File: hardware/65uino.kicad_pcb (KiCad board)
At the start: 2 copper layers, 74.9 x 53.3 mm, 58 parts, among them J1 Barrel_Jack_MountingPin, J2 USB_B_Micro, J3 OLED, SW1 RST, SW2 BTN, U1 R6507, U2 NC/74HC04, U3 6532, U4 w27C512, U5 MIC5504-3.3YM5, U6 LM1117-5.0, U7 SN74LVC1G14DBVR, X1 1MHz, Y1 NC/1Mhz

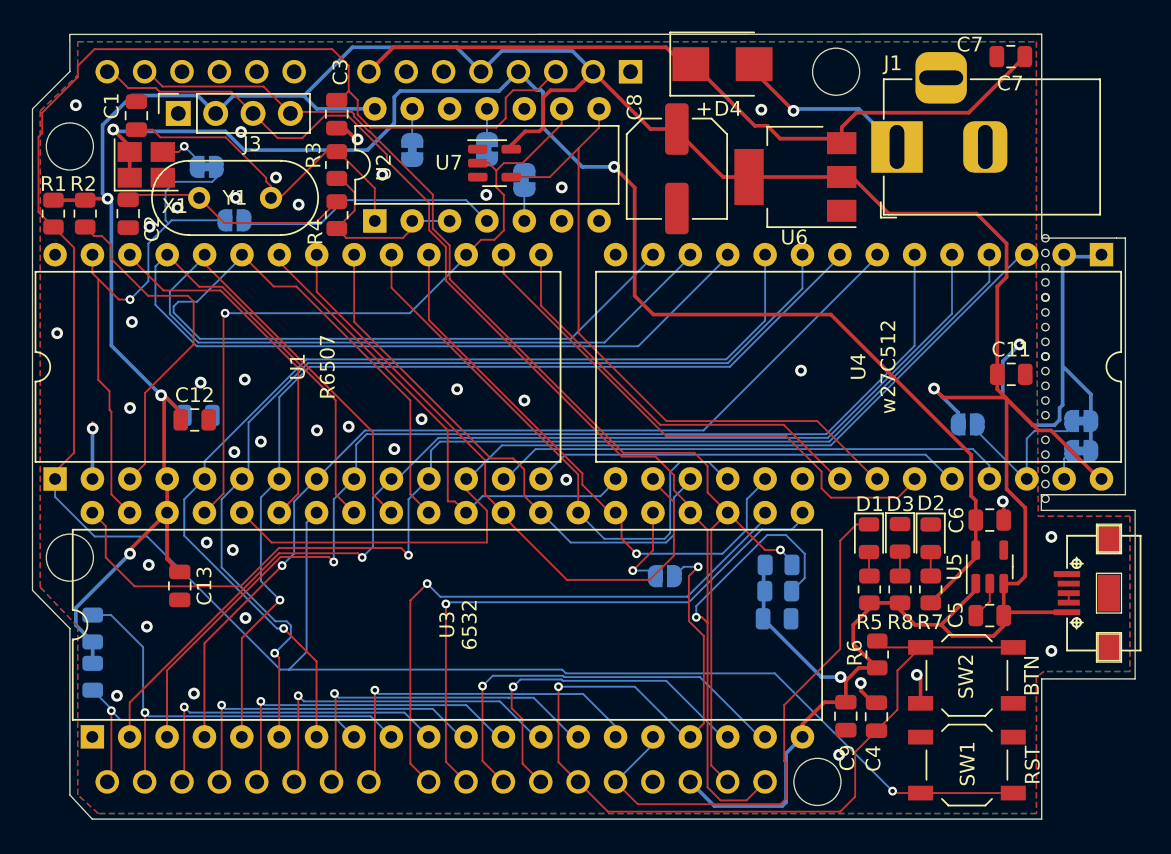
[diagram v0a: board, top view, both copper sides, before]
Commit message: Manufacturing improvements
MicroUSB changed to Amphenol 10118194
5V regulator capacitors changed to 1206 10uF
LCSC Parts numbers added
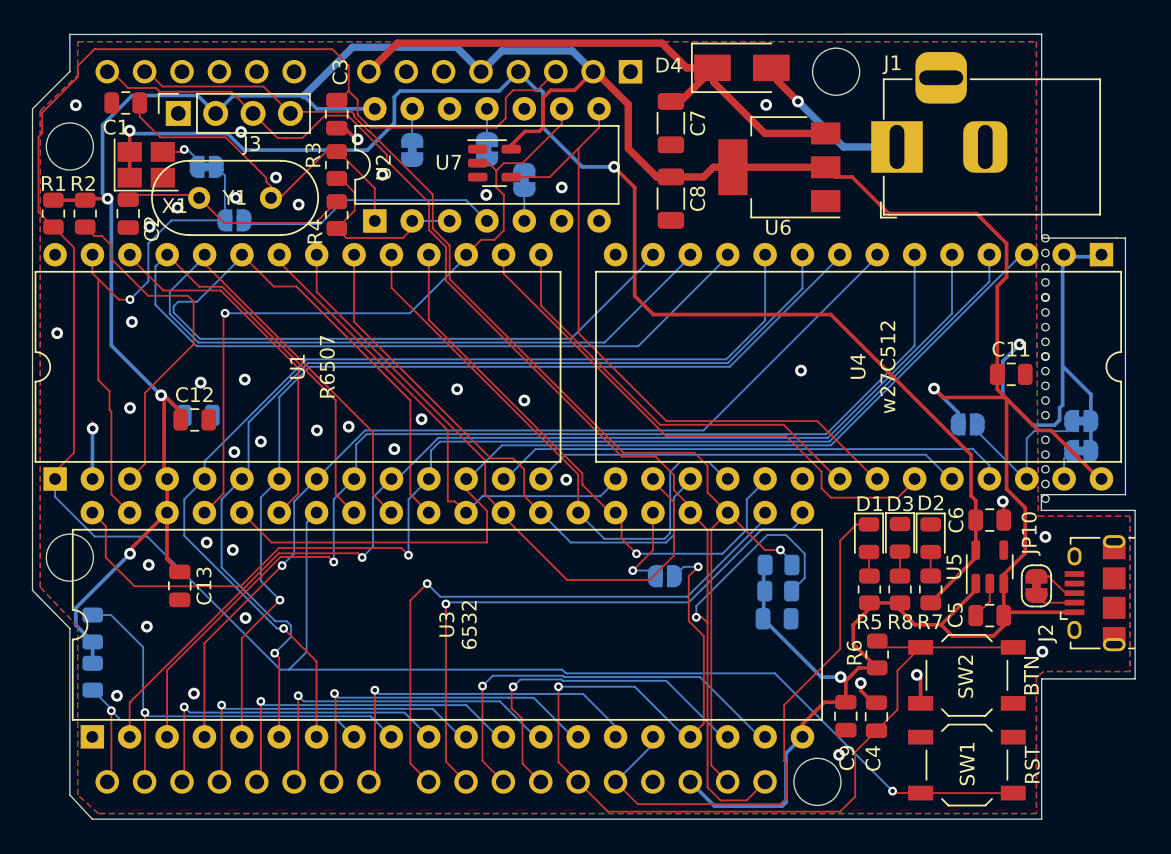
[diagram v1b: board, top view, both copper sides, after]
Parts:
- added JP10: SolderJumper_2_Bridged, Jumper:SolderJumper-2_P1.3mm_Bridged_RoundedPad1.0x1.5mm, F.Cu at (170.2, 86.0)
- A1: value Arduino Footprint -> NC/Arduino Footprint
- C7: value C_Input -> 10uF; footprint Capacitor_SMD:C_0805_2012Metric -> Capacitor_SMD:C_1206_3216Metric
- C8: value 47uF -> 10uF; footprint Capacitor_SMD:CP_Elec_6.3x7.7 -> Capacitor_SMD:C_1206_3216Metric
- D1: value LED -> GREEN LED
- D2: value LED -> RED LED
- D3: value LED -> WHITE LED
- D4: footprint Diode_SMD:D_SMB -> Diode_SMD:D_SMA
- J2: footprint Connector_USB:USB-B-MICRO-SMD_V03-fixed -> Connector_USB:USB_Micro-B_Amphenol_10118194_Horizontal
- moved C7 23.5 mm to (145.3, 54.6), turned to -90 degrees
- moved C8 2.07 mm to (145.3, 59.7)
- moved D4 1.35 mm to (150.2, 50.8)
- moved U6 1.28 mm to (152.7, 57.6)
- moved C1 1.13 mm to (108.3, 53.2), turned to 180 degrees
- moved J2 0.94 mm to (174.2, 86.5), turned to 90 degrees
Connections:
- J2 pad 3: Net-(J2-Pad2) -> Net-(J2-Pad3)
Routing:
- net /VIN: track 49.9 -> 38.2 mm
- net /PHI0: track 38.3 -> 35.4 mm
- net Net-(J2-Pad3): track 0.00 -> 2.45 mm
- net +5V: track 238.4 -> 240.8 mm
- net Net-(J2-Pad2): track 0.65 -> 2.79 mm
- net +3V3: track 92.9 -> 91.2 mm
- net Net-(D4-Pad2): track 12.2 -> 10.9 mm
- net Net-(C1-Pad1): track 21.9 -> 22.9 mm
- net Net-(U3-Pad25): track 6.19 -> 5.65 mm

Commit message: Minor PCB update
Gerbers regenerated
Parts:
- moved SW1 0.37 mm to (165.5, 98.6)
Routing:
- net +5V: track 240.8 -> 237.0 mm
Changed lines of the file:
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@@
     (fp_line (start 1.6 -0.8) (end 1.6 0.8) (layer "F.Fab") (width 0.1))
     (fp_line (start 1.6 0.8) (end -1.6 0.8) (layer "F.Fab") (width 0.1))
-    (pad "1" smd roundrect (at -1.475 0 270) (size 1.15 1.8) (layers "F.Cu" "F.Paste" "F.Mask") (roundrect_rratio 0.217391)
+    (pad "1" smd roundrect (at -1.475 0 270) (size 1.15 1.8) (layers "F.Cu" "F.Paste" "F.Mask") (roundrect_rratio 0.2173913043)
       (net 70 "/VIN") (pintype "passive"))
-    (pad "2" smd roundrect (at 1.475 0 270) (size 1.15 1.8) (layers "F.Cu" "F.Paste" "F.Mask") (roundrect_rratio 0.217391)
+    (pad "2" smd roundrect (at 1.475 0 270) (size 1.15 1.8) (layers "F.Cu" "F.Paste" "F.Mask") (roundrect_rratio 0.2173913043)
       (net 3 "GND") (pintype "passive"))
     (model "${KICAD6_3DMODEL_DIR}/Capacitor_SMD.3dshapes/C_1206_3216Metric.wrl"
@@
     (fp_line (start -1.6 -0.8) (end 1.6 -0.8) (layer "F.Fab") (width 0.1))
     (fp_line (start 1.6 -0.8) (end 1.6 0.8) (layer "F.Fab") (width 0.1))
-    (pad "1" smd roundrect (at -1.475 0 270) (size 1.15 1.8) (layers "F.Cu" "F.Paste" "F.Mask") (roundrect_rratio 0.217391)
+    (pad "1" smd roundrect (at -1.475 0 270) (size 1.15 1.8) (layers "F.Cu" "F.Paste" "F.Mask") (roundrect_rratio 0.2173913043)
       (net 2 "+5V") (pintype "passive"))
-    (pad "2" smd roundrect (at 1.475 0 270) (size 1.15 1.8) (layers "F.Cu" "F.Paste" "F.Mask") (roundrect_rratio 0.217391)
+    (pad "2" smd roundrect (at 1.475 0 270) (size 1.15 1.8) (layers "F.Cu" "F.Paste" "F.Mask") (roundrect_rratio 0.2173913043)
       (net 3 "GND") (pintype "passive"))
     (model "${KICAD6_3DMODEL_DIR}/Capacitor_SMD.3dshapes/C_1206_3216Metric.wrl"
@@
   )
   (footprint "Button_Switch_SMD:SW_SPST_TL3342" (layer "F.Cu")
-    (at 165.4556 98.1812)
+    (at 165.4556 98.552)
     (descr "Low-profile SMD Tactile Switch, https://www.e-switch.com/system/asset/product_line/data_sheet/165/TL3342.pdf")
     (tags "SPST Tactile Switch")
@@
   (segment (start 110.8964 73.2536) (end 110.6932 73.0504) (width 0.25) (layer "F.Cu") (net 2))
   (segment (start 149.5548 57.5564) (end 148.2166 57.5564) (width 0.5) (layer "F.Cu") (net 2))
+  (segment (start 166.9796 73.2028) (end 166.9288 73.2536) (width 0.25) (layer "F.Cu") (net 2))
   (segment (start 166.055 86.294) (end 163.703 88.646) (width 0.25) (layer "F.Cu") (net 2))
   (segment (start 154.2796 96.266) (end 154.2796 95.4024) (width 0.25) (layer "F.Cu") (net 2))
@@
   (segment (start 154.2796 95.4024) (end 155.7732 93.9088) (width 0.25) (layer "F.Cu") (net 2))
   (segment (start 157.6578 58.2168) (end 156.5152 58.2168) (width 0.25) (layer "F.Cu") (net 2))
-  (segment (start 163.83 73.2028) (end 163.2204 72.5932) (width 0.25) (layer "F.Cu") (net 2))
   (segment (start 110.8964 78.5268) (end 110.8964 73.2536) (width 0.25) (layer "F.Cu") (net 2))
   (segment (start 167.955 88.712) (end 167.259 89.408) (width 0.25) (layer "F.Cu") (net 2))
@@
   (segment (start 144.3718 58.215) (end 142.4432 56.2864) (width 0.5) (layer "F.Cu") (net 2))
   (segment (start 145.3388 58.215) (end 144.3718 58.215) (width 0.5) (layer "F.Cu") (net 2))
-  (segment (start 168.0718 73.2028) (end 163.83 73.2028) (width 0.25) (layer "F.Cu") (net 2))
   (segment (start 156.972 92.202) (end 157.226 92.456) (width 0.25) (layer "F.Cu") (net 2))
   (segment (start 167.955 85.2322) (end 167.955 85.8465) (width 0.25) (layer "F.Cu") (net 2))
@@
   (segment (start 168.148 79.426827) (end 169.418 80.696827) (width 0.25) (layer "F.Cu") (net 2))
   (segment (start 136.398 55.118) (end 136.652 54.864) (width 0.25) (layer "F.Cu") (net 2))
+  (segment (start 168.0718 73.2028) (end 166.9796 73.2028) (width 0.25) (layer "F.Cu") (net 2))
   (segment (start 110.8964 73.0504) (end 110.6932 73.0504) (width 0.25) (layer "F.Cu") (net 2))
   (segment (start 103.378 59.7935) (end 105.537 59.7935) (width 0.25) (layer "F.Cu") (net 2))
@@
   (segment (start 111.0996 81.026) (end 108.585 83.5406) (width 0.25) (layer "F.Cu") (net 2))
   (segment (start 169.418 80.696827) (end 169.418 83.7692) (width 0.25) (layer "F.Cu") (net 2))
-  (via (at 163.2204 72.5932) (size 0.8) (drill 0.4) (layers "F.Cu" "B.Cu") (net 2))
+  (via (at 166.9288 73.2536) (size 0.8) (drill 0.4) (layers "F.Cu" "B.Cu") (net 2))
   (via (at 107.061 59.69) (size 0.8) (drill 0.4) (layers "F.Cu" "B.Cu") (net 2))
   (via (at 108.585 83.82) (size 0.8) (drill 0.4) (layers "F.Cu" "B.Cu") (net 2))
@@
   (segment (start 151.638 84.582) (end 151.638 86.36) (width 0.25) (layer "B.Cu") (net 2))
   (segment (start 151.6024 88.2396) (end 155.5648 92.202) (width 0.25) (layer "B.Cu") (net 2))
-  (segment (start 164.8564 75.0316) (end 164.8564 74.2292) (width 0.25) (layer "B.Cu") (net 2))
   (segment (start 112.268 74.422) (end 110.8964 73.0504) (width 0.25) (layer "B.Cu") (net 2))
   (segment (start 125.217 53.584) (end 121.275 53.584) (width 0.25) (layer "B.Cu") (net 2))
+  (segment (start 165.835872 73.2536) (end 166.9288 73.2536) (width 0.25) (layer "B.Cu") (net 2))
   (segment (start 123.698 49.403) (end 130.7744 49.403) (width 0.5) (layer "B.Cu") (net 2))
   (segment (start 107.315 59.944) (end 107.315 69.6722) (width 0.25) (layer "B.Cu") (net 2))
@@
   (segment (start 106.7175 59.3465) (end 107.061 59.69) (width 0.25) (layer "B.Cu") (net 2))
   (segment (start 130.7744 49.403) (end 132.4356 51.0642) (width 0.5) (layer "B.Cu") (net 2))
-  (segment (start 164.8564 74.2292) (end 163.2204 72.5932) (width 0.25) (layer "B.Cu") (net 2))
+  (segment (start 164.8564 74.233072) (end 165.835872 73.2536) (width 0.25) (layer "B.Cu") (net 2))
+  (segment (start 164.8564 75.0316) (end 164.8564 74.233072) (width 0.25) (layer "B.Cu") (net 2))
   (segment (start 106.045 89.8125) (end 106.045 91.266) (width 0.25) (layer "B.Cu") (net 2))
   (segment (start 113.1824 52.6796) (end 108.728802 52.6796) (width 0.25) (layer "B.Cu") (net 2))
@@
   (segment (start 167.955 80.325) (end 167.894 80.264) (width 0.25) (layer "F.Cu") (net 3))
   (segment (start 167.955 81.534) (end 167.955 80.325) (width 0.25) (layer "F.Cu") (net 3))
-  (via (at 156.7688 97.4852) (size 0.8) (drill 0.4) (layers "F.Cu" "B.Cu") (net 3))
+  (via (at 157.3276 97.9932) (size 0.8) (drill 0.4) (layers "F.Cu" "B.Cu") (net 3))
   (via (at 126.5428 76.708) (size 0.8) (drill 0.4) (layers "F.Cu" "B.Cu") (net 3))
   (via (at 125.73 58.0644) (size 0.8) (drill 0.4) (layers "F.Cu" "B.Cu") (net 3))
@@
   (segment (start 106.172 49.53) (end 105.029 50.673) (width 0.127) (layer "F.Cu") (net 71))
   (segment (start 134.62 52.324) (end 134.112 52.832) (width 0.127) (layer "F.Cu") (net 71))
-  (segment (start 160.401 99.949) (end 160.5332 100.0812) (width 0.127) (layer "F.Cu") (net 71))
   (segment (start 124.052602 52.983402) (end 123.444 52.3748) (width 0.127) (layer "F.Cu") (net 71))
   (segment (start 137.5156 51.0642) (end 136.2558 52.324) (width 0.127) (layer "F.Cu") (net 71))
   (segment (start 105.029 50.673) (end 105.029 51.435) (width 0.127) (layer "F.Cu") (net 71))
-  (segment (start 168.6056 100.0812) (end 162.3056 100.0812) (width 0.127) (layer "F.Cu") (net 71))
   (segment (start 104.775 63.0155) (end 104.775 76.962) (width 0.127) (layer "F.Cu") (net 71))
+  (segment (start 160.904 100.452) (end 162.3056 100.452) (width 0.127) (layer "F.Cu") (net 71))
   (segment (start 122.7176 53.1012) (end 123.444 52.3748) (width 0.127) (layer "F.Cu") (net 71))
-  (segment (start 160.5332 100.0812) (end 162.3056 100.0812) (width 0.127) (layer "F.Cu") (net 71))
   (segment (start 103.378 61.6185) (end 104.775 63.0155) (width 0.127) (layer "F.Cu") (net 71))
   (segment (start 102.362 55.499) (end 102.362 60.6025) (width 0.127) (layer "F.Cu") (net 71))
@@
   (segment (start 123.444 52.3748) (end 123.444 50.6476) (width 0.127) (layer "F.Cu") (net 71))
   (segment (start 123.444 50.6476) (end 122.3264 49.53) (width 0.127) (layer "F.Cu") (net 71))
+  (segment (start 168.6056 100.452) (end 162.3056 100.452) (width 0.127) (layer "F.Cu") (net 71))
   (segment (start 102.616 55.245) (end 102.362 55.499) (width 0.127) (layer "F.Cu") (net 71))
   (segment (start 122.3264 49.53) (end 106.172 49.53) (width 0.127) (layer "F.Cu") (net 71))
+  (segment (start 160.401 99.949) (end 160.904 100.452) (width 0.127) (layer "F.Cu") (net 71))
   (segment (start 134.112 52.832) (end 134.112 54.229) (width 0.127) (layer "F.Cu") (net 71))
   (via (at 160.401 99.949) (size 0.6) (drill 0.3) (layers "F.Cu" "B.Cu") (net 71))

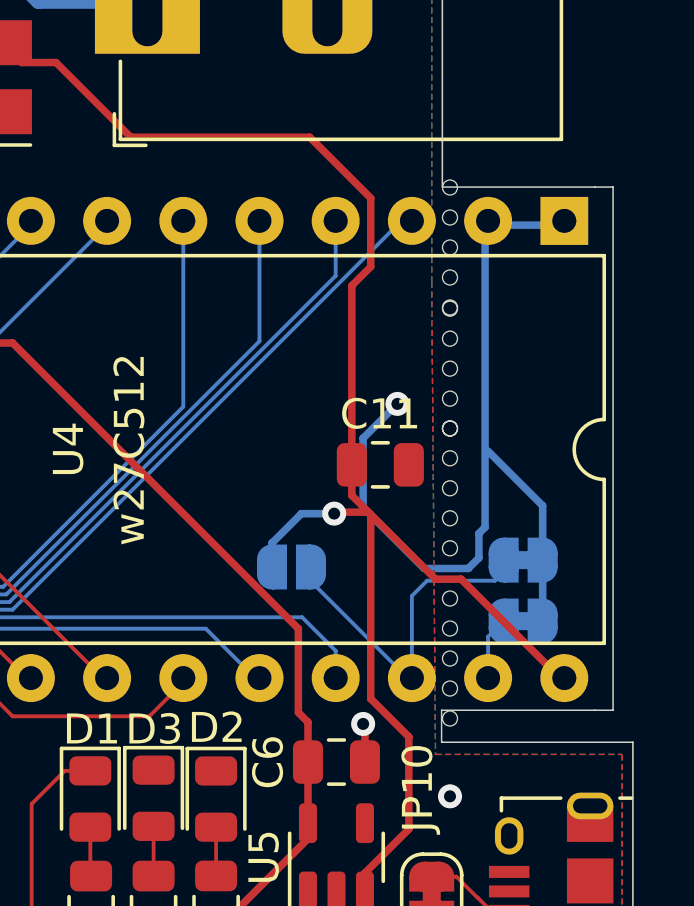
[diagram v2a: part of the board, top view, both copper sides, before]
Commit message: Software and hardware serial flow control + mouse bites removed
Mouse bites removed due to manufacturer policies - like "this looks like two boards"-surcharge.
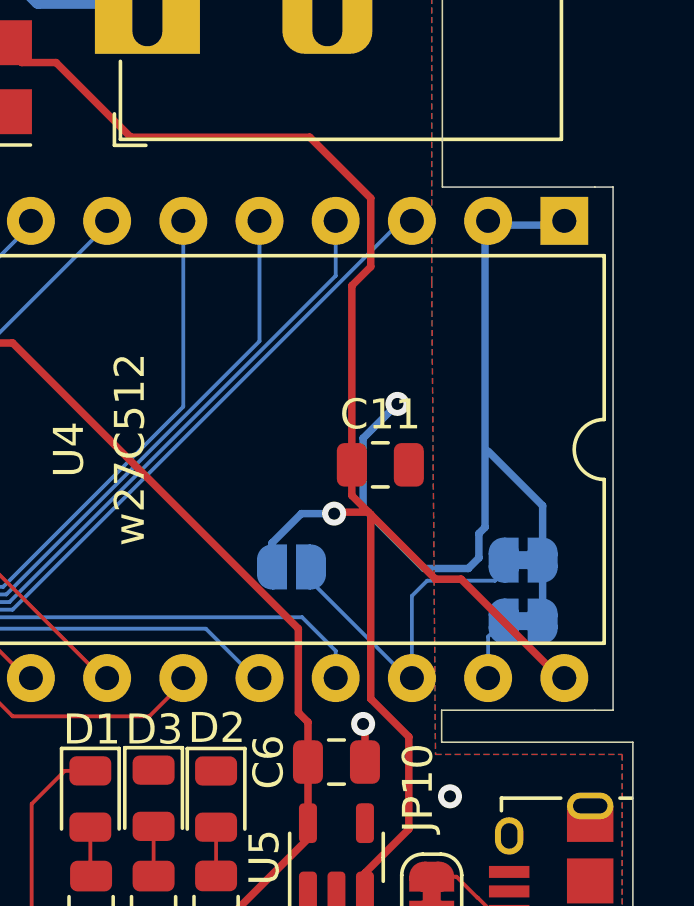
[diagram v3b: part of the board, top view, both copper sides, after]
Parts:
- removed REF** (x4): Mousebite, 65uino:Mousebite
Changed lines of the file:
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@@
     )
-  )
-  (footprint "65uino:Mousebite" (layer "F.Cu")
-    (at 170.7896 76.0832)
-    (fp_text reference "REF**" (at 0 -0.5 unlocked) (layer "F.SilkS") hide
-      (effects (font (size 1 1) (thickness 0.15)))
-    )
-    (fp_text value "Mousebite" (at 0 1 unlocked) (layer "F.Fab")
-      (effects (font (size 1 1) (thickness 0.15)))
-    )
-    (fp_text user "${REFERENCE}" (at 0 2.5 unlocked) (layer "F.Fab")
-      (effects (font (size 1 1) (thickness 0.15)))
-    )
-    (pad "" np_thru_hole circle (at 0 1) (size 0.5 0.5) (drill 0.5) (layers F&B.Cu *.Mask))
-    (pad "" np_thru_hole circle (at 0 2) (size 0.5 0.5) (drill 0.5) (layers F&B.Cu *.Mask))
-    (pad "" np_thru_hole circle (at 0 4) (size 0.5 0.5) (drill 0.5) (layers F&B.Cu *.Mask))
-    (pad "" np_thru_hole circle (at 0 3) (size 0.5 0.5) (drill 0.5) (layers F&B.Cu *.Mask))
-    (pad "" np_thru_hole circle (at 0 0) (size 0.5 0.5) (drill 0.5) (layers F&B.Cu *.Mask))
   )
   (footprint "Capacitor_SMD:C_0805_2012Metric" (layer "F.Cu")
@@
       (rotate (xyz 0 0 0))
     )
-  )
-  (footprint "65uino:Mousebite" (layer "F.Cu")
-    (at 170.7896 70.4088)
-    (fp_text reference "REF**" (at 0 -0.5 unlocked) (layer "F.SilkS") hide
-      (effects (font (size 1 1) (thickness 0.15)))
-    )
-    (fp_text value "Mousebite" (at 0 1 unlocked) (layer "F.Fab") hide
-      (effects (font (size 1 1) (thickness 0.15)))
-    )
-    (fp_text user "${REFERENCE}" (at 0 2.5 unlocked) (layer "F.Fab") hide
-      (effects (font (size 1 1) (thickness 0.15)))
-    )
-    (pad "" np_thru_hole circle (at 0 4) (size 0.5 0.5) (drill 0.5) (layers F&B.Cu *.Mask))
-    (pad "" np_thru_hole circle (at 0 2) (size 0.5 0.5) (drill 0.5) (layers F&B.Cu *.Mask))
-    (pad "" np_thru_hole circle (at 0 1) (size 0.5 0.5) (drill 0.5) (layers F&B.Cu *.Mask))
-    (pad "" np_thru_hole circle (at 0 3) (size 0.5 0.5) (drill 0.5) (layers F&B.Cu *.Mask))
-    (pad "" np_thru_hole circle (at 0 0) (size 0.5 0.5) (drill 0.5) (layers F&B.Cu *.Mask))
   )
   (footprint "Connector_BarrelJack:BarrelJack_Horizontal" (layer "F.Cu")
@@
     )
   )
-  (footprint "65uino:Mousebite" (layer "F.Cu")
-    (at 170.7896 66.421)
-    (fp_text reference "REF**" (at 0 -0.5 unlocked) (layer "F.SilkS") hide
-      (effects (font (size 1 1) (thickness 0.15)))
-    )
-    (fp_text value "Mousebite" (at 0 1 unlocked) (layer "F.Fab") hide
-      (effects (font (size 1 1) (thickness 0.15)))
-    )
-    (fp_text user "${REFERENCE}" (at 0 2.5 unlocked) (layer "F.Fab") hide
-      (effects (font (size 1 1) (thickness 0.15)))
-    )
-    (pad "" np_thru_hole circle (at 0 2) (size 0.5 0.5) (drill 0.5) (layers F&B.Cu *.Mask))
-    (pad "" np_thru_hole circle (at 0 1) (size 0.5 0.5) (drill 0.5) (layers F&B.Cu *.Mask))
-    (pad "" np_thru_hole circle (at 0 4) (size 0.5 0.5) (drill 0.5) (layers F&B.Cu *.Mask))
-    (pad "" np_thru_hole circle (at 0 0) (size 0.5 0.5) (drill 0.5) (layers F&B.Cu *.Mask))
-    (pad "" np_thru_hole circle (at 0 3) (size 0.5 0.5) (drill 0.5) (layers F&B.Cu *.Mask))
-  )
   (footprint "Capacitor_SMD:C_0805_2012Metric" (layer "F.Cu")
     (at 167.005 88.0212 180)
@@
     )
   )
-  (footprint "65uino:Mousebite" (layer "F.Cu")
-    (at 170.7896 62.3824)
-    (fp_text reference "REF**" (at 0 -0.5 unlocked) (layer "F.SilkS") hide
-      (effects (font (size 1 1) (thickness 0.15)))
-    )
-    (fp_text value "Mousebite" (at 0 1 unlocked) (layer "F.Fab") hide
-      (effects (font (size 1 1) (thickness 0.15)))
-    )
-    (fp_text user "${REFERENCE}" (at 0 2.5 unlocked) (layer "F.Fab") hide
-      (effects (font (size 1 1) (thickness 0.15)))
-    )
-    (pad "" np_thru_hole circle (at 0 0) (size 0.5 0.5) (drill 0.5) (layers F&B.Cu *.Mask))
-    (pad "" np_thru_hole circle (at 0 2) (size 0.5 0.5) (drill 0.5) (layers F&B.Cu *.Mask))
-    (pad "" np_thru_hole circle (at 0 3) (size 0.5 0.5) (drill 0.5) (layers F&B.Cu *.Mask))
-    (pad "" np_thru_hole circle (at 0 4) (size 0.5 0.5) (drill 0.5) (layers F&B.Cu *.Mask))
-    (pad "" np_thru_hole circle (at 0 1) (size 0.5 0.5) (drill 0.5) (layers F&B.Cu *.Mask))
-  )
   (footprint "Capacitor_SMD:C_0805_2012Metric" (layer "B.Cu")
